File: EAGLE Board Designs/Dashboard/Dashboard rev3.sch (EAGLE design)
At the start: 61 parts, among them J1 AVR-ISP-HEADER, J2 JUMPER0603, X1 CONNECTOR-8NANO, X3 CONNECTOR-4NANO, X4 CONNECTOR-6NANO

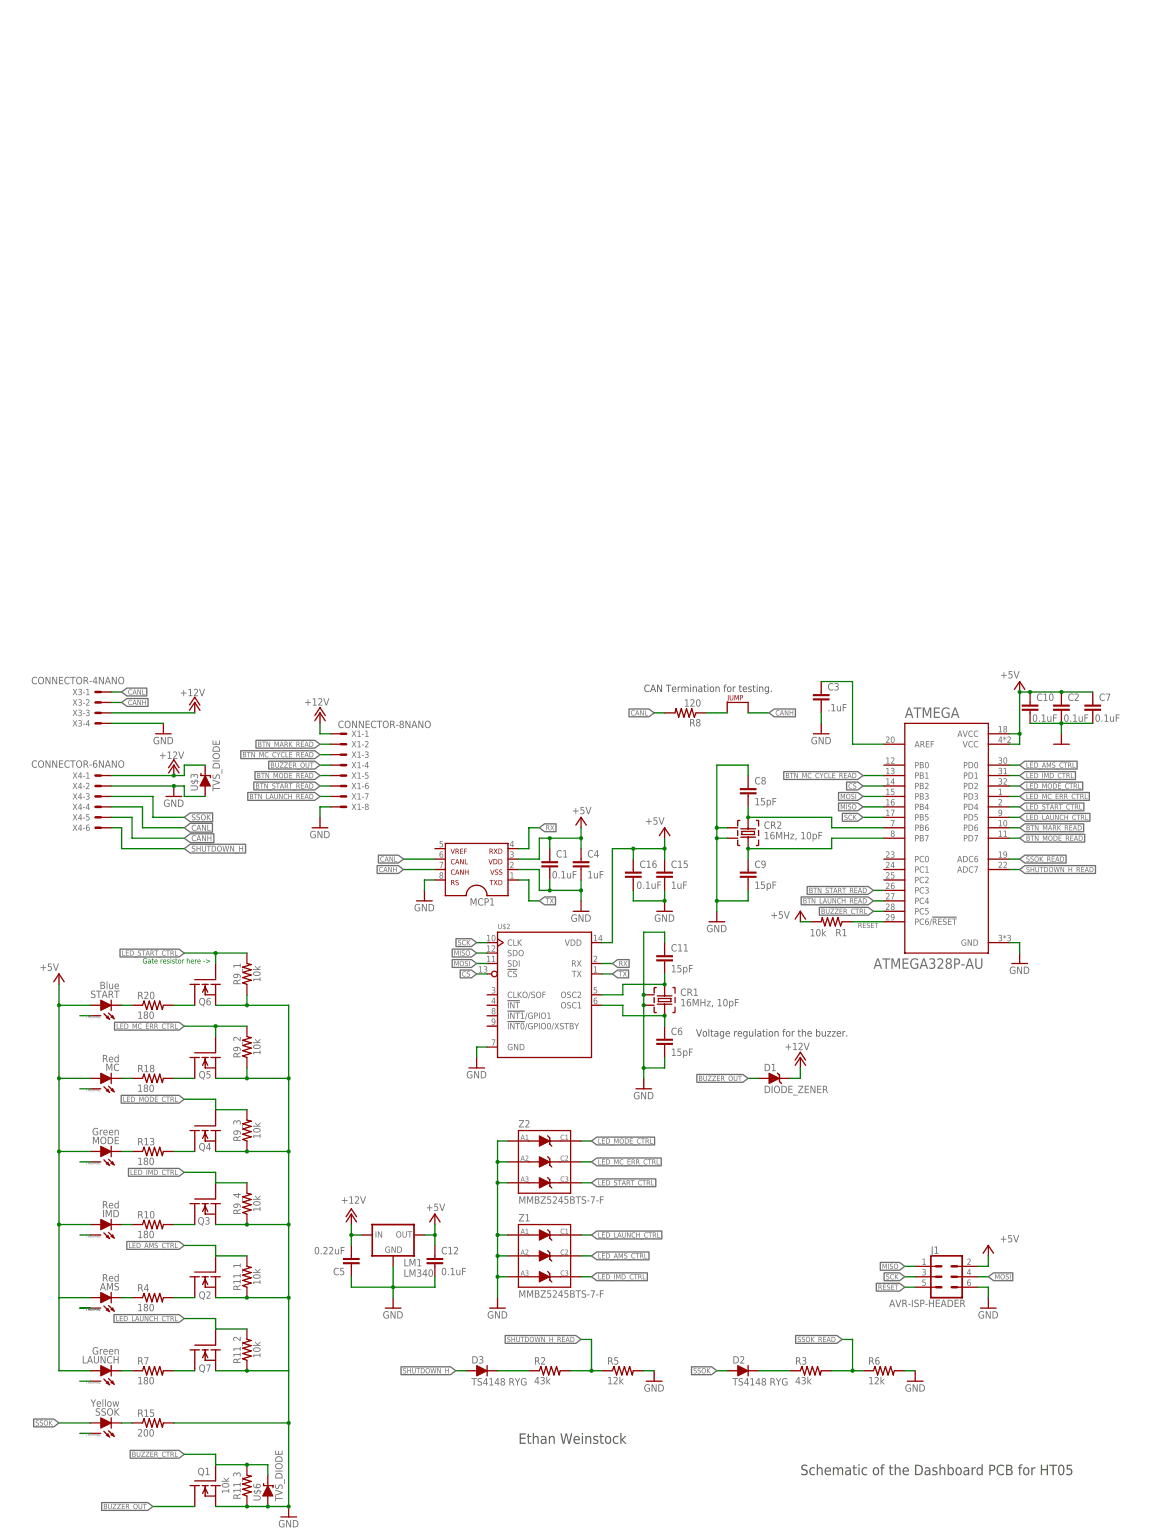
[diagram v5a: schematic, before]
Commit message: MCP 2551 -> MCP2562FD in Rev3 File
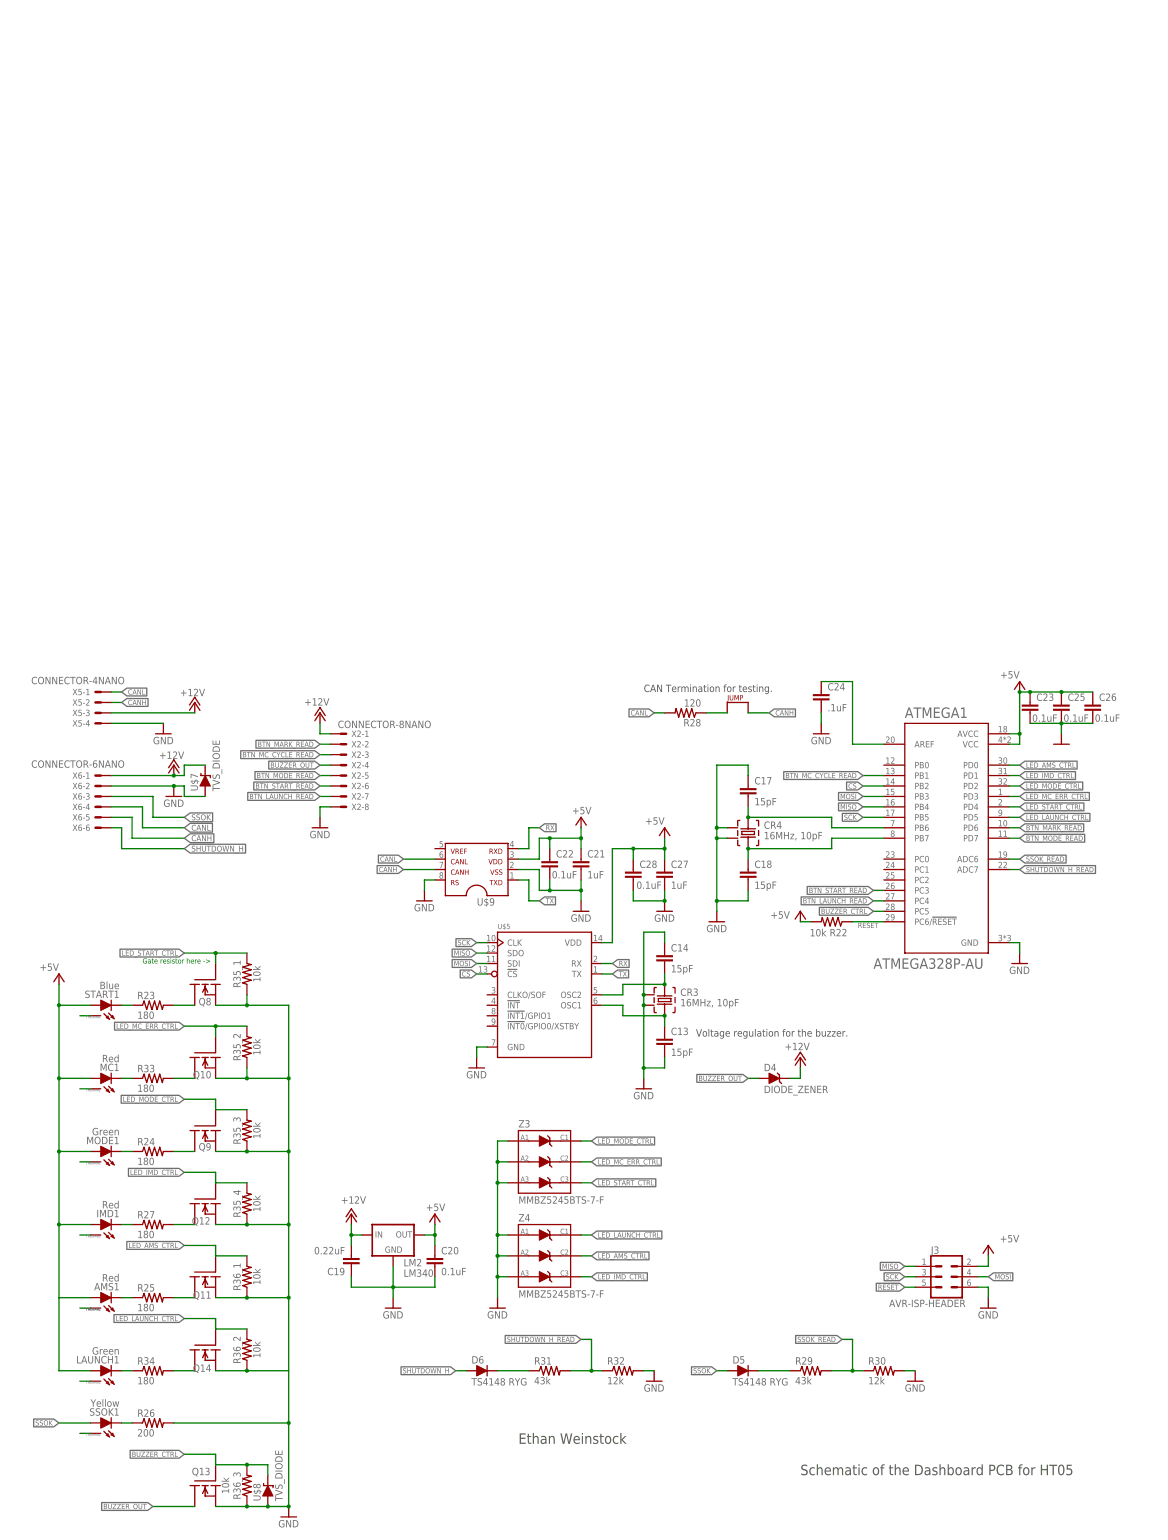
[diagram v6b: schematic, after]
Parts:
- removed MCP1: MCP2551, HyTechDevices:MCP2551
- added U$9: MCP2562FD, HyTechDevices:MCP2562FD
- renumbered AMS to AMS1, ATMEGA to ATMEGA1, C1 to C22, C10 to C23, C11 to C14, C12 to C20, C15 to C27, C16 to C28, C2 to C25, C3 to C24, C4 to C21, C5 to C19, C6 to C13, C7 to C26, C8 to C17, C9 to C18, CR1 to CR3, CR2 to CR4, D1 to D4, D2 to D5, D3 to D6, IMD to IMD1, J1 to J3, J2 to J4, LAUNCH to LAUNCH1, LM1 to LM2, MC to MC1, MODE to MODE1, Q1 to Q13, Q2 to Q11, Q3 to Q12, Q4 to Q9, Q5 to Q10, Q6 to Q8, Q7 to Q14, R1 to R22, R10 to R27, R11 to R36, R13 to R24, R15 to R26, R18 to R33, R2 to R31, R20 to R23, R3 to R29, R4 to R25, R5 to R32, R6 to R30, R7 to R34, R8 to R28, R9 to R35, SSOK to SSOK1, START to START1, U$2 to U$5, U$3 to U$7, U$6 to U$8, X1 to X2, X3 to X5, X4 to X6, Z1 to Z4, Z2 to Z3
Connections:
- net GND1 renamed GND2
- removed net N$30: C14.2, CR3.1, U$5.OSC2
- new net N$42: C14.2, C21.2, C22.2, CR3.1, U$5.OSC2, U$9.2
- net +5V: now also U$9.3; no longer MCP1.3
- net CANH: now also U$9.7; no longer MCP1.7
- net CANL: now also U$9.6; no longer MCP1.6
- net GND: now also U$9.8; no longer C21.2, C22.2, MCP1.2, MCP1.8
- net RX: now also U$9.4; no longer MCP1.4
- net TX: now also U$9.1; no longer MCP1.1

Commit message: Finished changes
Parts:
- removed J3: AVR-ISP-HEADER, HyTechDevices:AVR-ISP-HEADER
- added X1: CONNECTOR-6NANO, HyTechDevices:CONNECTOR-6NANO
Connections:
- net +5V: now also X1-2.S; no longer J3.2
- net GND: now also X1-6.S; no longer J3.6
- net MISO: now also X1-1.S; no longer J3.1
- net MOSI: now also X1-4.S; no longer J3.4
- net RESET: now also X1-5.S; no longer J3.5
- net SCK: now also X1-3.S; no longer J3.3
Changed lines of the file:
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@@
 <part name="C26" library="HyTechDevices" deviceset="CAP" device="0603-CAP" value="0.1uF"/>
 <part name="GND29" library="HyTechSymbols" deviceset="GND" device=""/>
-<part name="J3" library="HyTechDevices" deviceset="AVR-ISP-HEADER" device="" package3d_urn="urn:adsk.eagle:package:22462/2"/>
 <part name="GND30" library="HyTechSymbols" deviceset="GND" device=""/>
 <part name="P+21" library="supply1" library_urn="urn:adsk.eagle:library:371" deviceset="+5V" device=""/>
@@
 <part name="R36" library="HyTechDevices" deviceset="CAT16-*4" device="_1%" technology="F" value="10k"/>
 <part name="U$9" library="HyTechDevices" deviceset="MCP2562FD" device=""/>
+<part name="X1" library="HyTechDevices" deviceset="CONNECTOR-6" device="NANO"/>
 </parts>
 <sheets>
@@
 </instance>
 <instance part="GND29" gate="1" x="259.08" y="193.04" smashed="yes"/>
-<instance part="J3" gate="G$1" x="231.14" y="63.5" smashed="yes">
-<attribute name="VALUE" x="217.17" y="56.134" size="1.778" layer="96"/>
-<attribute name="NAME" x="227.33" y="69.088" size="1.778" layer="95"/>
-</instance>
-<instance part="GND30" gate="1" x="241.3" y="55.88" smashed="yes">
-<attribute name="VALUE" x="238.76" y="53.34" size="1.778" layer="96"/>
-</instance>
-<instance part="P+21" gate="1" x="241.3" y="71.12" smashed="yes">
-<attribute name="VALUE" x="244.094" y="71.882" size="1.778" layer="96"/>
+<instance part="GND30" gate="1" x="236.22" y="86.36" smashed="yes">
+<attribute name="VALUE" x="233.68" y="83.82" size="1.778" layer="96"/>
+</instance>
+<instance part="P+21" gate="1" x="231.14" y="81.28" smashed="yes">
+<attribute name="VALUE" x="228.854" y="82.042" size="1.778" layer="96"/>
 </instance>
 <instance part="D4" gate="G$1" x="190.5" y="111.76" smashed="yes">
@@
 <instance part="U$9" gate="G$1" x="124.46" y="167.64" smashed="yes" rot="R180">
 <attribute name="NAME" x="121.285" y="155.575" size="1.778" layer="95" rot="R180"/>
+</instance>
+<instance part="X1" gate="-1" x="259.08" y="76.2" smashed="yes">
+<attribute name="NAME" x="261.62" y="75.438" size="1.524" layer="95"/>
+<attribute name="VALUE" x="253.238" y="72.517" size="1.778" layer="96"/>
+</instance>
+<instance part="X1" gate="-2" x="259.08" y="78.74" smashed="yes">
+<attribute name="NAME" x="261.62" y="77.978" size="1.524" layer="95"/>
+</instance>
+<instance part="X1" gate="-3" x="259.08" y="81.28" smashed="yes">
+<attribute name="NAME" x="261.62" y="80.518" size="1.524" layer="95"/>
+</instance>
+<instance part="X1" gate="-4" x="259.08" y="83.82" smashed="yes">
+<attribute name="NAME" x="261.62" y="83.058" size="1.524" layer="95"/>
+</instance>
+<instance part="X1" gate="-5" x="259.08" y="86.36" smashed="yes">
+<attribute name="NAME" x="261.62" y="85.598" size="1.524" layer="95"/>
+</instance>
+<instance part="X1" gate="-6" x="259.08" y="88.9" smashed="yes">
+<attribute name="NAME" x="261.62" y="88.138" size="1.524" layer="95"/>
 </instance>
 </instances>
@@
 <pinref part="GND29" gate="1" pin="GND"/>
 <wire x1="259.08" y1="198.12" x2="259.08" y2="195.58" width="0.1524" layer="91"/>
-</segment>
-<segment>
-<pinref part="GND30" gate="1" pin="GND"/>
-<wire x1="241.3" y1="58.42" x2="241.3" y2="60.96" width="0.1524" layer="91"/>
-<pinref part="J3" gate="G$1" pin="6"/>
-<wire x1="241.3" y1="60.96" x2="238.76" y2="60.96" width="0.1524" layer="91"/>
 </segment>
 <segment>
@@
 <pinref part="GND36" gate="1" pin="GND"/>
 </segment>
+<segment>
+<pinref part="X1" gate="-6" pin="S"/>
+<pinref part="GND30" gate="1" pin="GND"/>
+<wire x1="256.54" y1="88.9" x2="236.22" y2="88.9" width="0.1524" layer="91"/>
+</segment>
 </net>
 <net name="+5V" class="0">
@@
 <segment>
 <pinref part="P+21" gate="1" pin="+5V"/>
-<wire x1="241.3" y1="68.58" x2="241.3" y2="66.04" width="0.1524" layer="91"/>
-<pinref part="J3" gate="G$1" pin="2"/>
-<wire x1="241.3" y1="66.04" x2="238.76" y2="66.04" width="0.1524" layer="91"/>
+<pinref part="X1" gate="-2" pin="S"/>
+<wire x1="256.54" y1="78.74" x2="231.14" y2="78.74" width="0.1524" layer="91"/>
 </segment>
 <segment>
@@
 </segment>
 <segment>
-<pinref part="J3" gate="G$1" pin="3"/>
-<wire x1="223.52" y1="63.5" x2="220.98" y2="63.5" width="0.1524" layer="91"/>
-<label x="220.98" y="63.5" size="1.27" layer="95" rot="R180" xref="yes"/>
+<wire x1="256.54" y1="81.28" x2="248.92" y2="81.28" width="0.1524" layer="91"/>
+<label x="248.92" y="81.28" size="1.27" layer="95" rot="R180" xref="yes"/>
+<pinref part="X1" gate="-3" pin="S"/>
 </segment>
 <segment>
@@
 </segment>
 <segment>
-<pinref part="J3" gate="G$1" pin="1"/>
-<wire x1="223.52" y1="66.04" x2="220.98" y2="66.04" width="0.1524" layer="91"/>
-<label x="220.98" y="66.04" size="1.27" layer="95" rot="R180" xref="yes"/>
+<wire x1="256.54" y1="76.2" x2="248.92" y2="76.2" width="0.1524" layer="91"/>
+<label x="248.92" y="76.2" size="1.27" layer="95" rot="R180" xref="yes"/>
+<pinref part="X1" gate="-1" pin="S"/>
 </segment>
 <segment>
@@
 </segment>
 <segment>
-<pinref part="J3" gate="G$1" pin="4"/>
-<wire x1="238.76" y1="63.5" x2="241.3" y2="63.5" width="0.1524" layer="91"/>
-<label x="241.3" y="63.5" size="1.27" layer="95" xref="yes"/>
+<wire x1="256.54" y1="83.82" x2="248.92" y2="83.82" width="0.1524" layer="91"/>
+<label x="248.92" y="83.82" size="1.27" layer="95" rot="R180" xref="yes"/>
+<pinref part="X1" gate="-4" pin="S"/>
 </segment>
 <segment>
@@
 </segment>
 <segment>
-<pinref part="J3" gate="G$1" pin="5"/>
-<wire x1="223.52" y1="60.96" x2="220.98" y2="60.96" width="0.1524" layer="91"/>
-<label x="220.98" y="60.96" size="1.27" layer="95" rot="R180" xref="yes"/>
+<wire x1="256.54" y1="86.36" x2="248.92" y2="86.36" width="0.1524" layer="91"/>
+<label x="248.92" y="86.36" size="1.27" layer="95" rot="R180" xref="yes"/>
+<pinref part="X1" gate="-5" pin="S"/>
 </segment>
 </net>
@@
 will not be understood (or retained) with this version.
 </note>
-<note version="8.3" severity="warning">
-Since Version 8.3, EAGLE supports the association of 3D packages
-with devices in libraries, schematics, and board files. Those 3D
-packages will not be understood (or retained) with this version.
-</note>
 </compatibility>

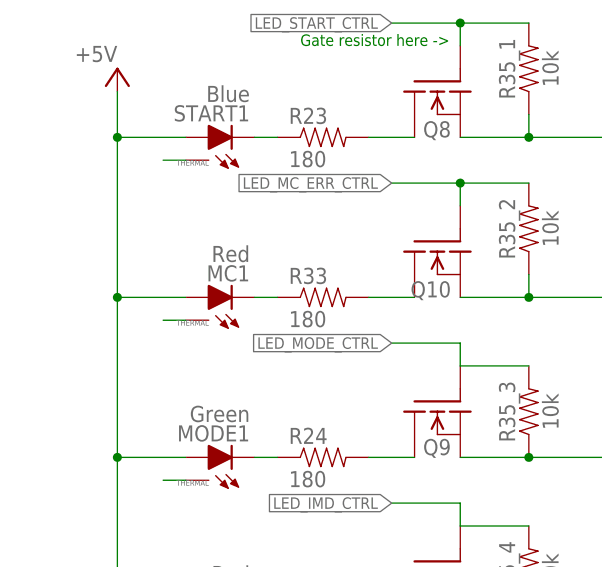
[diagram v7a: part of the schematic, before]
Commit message: Changed MCerror to green
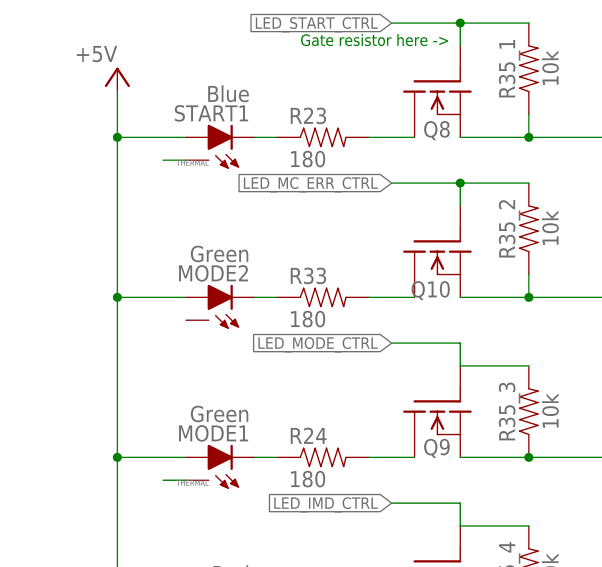
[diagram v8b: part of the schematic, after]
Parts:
- MODE2: value Red -> Green
- renumbered MC1 to MODE2
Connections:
- net THERMAL: no longer MODE2.X
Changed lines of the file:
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@@
 <part name="R28" library="HyTechDevices" deviceset="RESISTOR" device="0603-RES" value="120"/>
 <part name="GND31" library="HyTechSymbols" deviceset="GND" device=""/>
-<part name="MC1" library="HyTechDevices" deviceset="XP-E2" device="XP-E2" value="Red"/>
 <part name="START1" library="HyTechDevices" deviceset="XP-E2" device="XP-E2" value="Blue"/>
 <part name="MODE1" library="HyTechDevices" deviceset="XP-E2" device="XP-E2" value="Green"/>
@@
 <part name="U$9" library="HyTechDevices" deviceset="MCP2562FD" device=""/>
 <part name="X1" library="HyTechDevices" deviceset="CONNECTOR-6" device="NANO"/>
+<part name="MODE2" library="HyTechDevices" deviceset="XP-E2" device="XP-E2" value="Green"/>
 </parts>
 <sheets>
@@
 <attribute name="VALUE" x="68.58" y="2.54" size="1.778" layer="96"/>
 </instance>
-<instance part="MC1" gate="G$1" x="25.4" y="111.76" smashed="yes" rot="R90">
-<attribute name="NAME" x="29.972" y="115.316" size="1.778" layer="95" rot="R180"/>
-<attribute name="VALUE" x="29.972" y="117.475" size="1.778" layer="96" rot="R180"/>
-</instance>
 <instance part="START1" gate="G$1" x="25.4" y="129.54" smashed="yes" rot="R90">
 <attribute name="NAME" x="29.972" y="133.096" size="1.778" layer="95" rot="R180"/>
@@
 <instance part="X1" gate="-6" x="259.08" y="88.9" smashed="yes">
 <attribute name="NAME" x="261.62" y="88.138" size="1.524" layer="95"/>
+</instance>
+<instance part="MODE2" gate="G$1" x="25.4" y="111.76" smashed="yes" rot="R90">
+<attribute name="NAME" x="29.972" y="115.316" size="1.778" layer="95" rot="R180"/>
+<attribute name="VALUE" x="29.972" y="117.475" size="1.778" layer="96" rot="R180"/>
 </instance>
 </instances>
@@
 </segment>
 <segment>
-<pinref part="MC1" gate="G$1" pin="X"/>
-<wire x1="22.86" y1="109.22" x2="20.32" y2="109.22" width="0.1524" layer="91"/>
-<label x="25.4" y="109.22" size="0.6096" layer="95" rot="R180"/>
-</segment>
-<segment>
 <pinref part="MODE1" gate="G$1" pin="X"/>
 <wire x1="22.86" y1="91.44" x2="20.32" y2="91.44" width="0.1524" layer="91"/>
@@
 <wire x1="15.24" y1="76.2" x2="15.24" y2="93.98" width="0.1524" layer="91"/>
 <wire x1="15.24" y1="93.98" x2="15.24" y2="111.76" width="0.1524" layer="91"/>
+<pinref part="P+19" gate="1" pin="+5V"/>
 <wire x1="15.24" y1="111.76" x2="15.24" y2="129.54" width="0.1524" layer="91"/>
-<pinref part="P+19" gate="1" pin="+5V"/>
 <wire x1="15.24" y1="129.54" x2="15.24" y2="134.62" width="0.1524" layer="91"/>
-<wire x1="15.24" y1="111.76" x2="22.86" y2="111.76" width="0.1524" layer="91"/>
-<junction x="15.24" y="111.76"/>
 <wire x1="22.86" y1="93.98" x2="15.24" y2="93.98" width="0.1524" layer="91"/>
 <junction x="15.24" y="93.98"/>
@@
 <junction x="15.24" y="129.54"/>
 <pinref part="START1" gate="G$1" pin="A"/>
-<pinref part="MC1" gate="G$1" pin="A"/>
 <pinref part="MODE1" gate="G$1" pin="A"/>
 <pinref part="IMD1" gate="G$1" pin="A"/>
 <pinref part="AMS1" gate="G$1" pin="A"/>
+<pinref part="MODE2" gate="G$1" pin="A"/>
+<wire x1="22.86" y1="111.76" x2="15.24" y2="111.76" width="0.1524" layer="91"/>
+<junction x="15.24" y="111.76"/>
 </segment>
 </net>
@@
 <wire x1="33.02" y1="58.42" x2="30.48" y2="58.42" width="0.1524" layer="91"/>
 <pinref part="AMS1" gate="G$1" pin="C"/>
-</segment>
-</net>
-<net name="N$28" class="0">
-<segment>
-<pinref part="MC1" gate="G$1" pin="C"/>
-<pinref part="R33" gate="G$1" pin="1"/>
-<wire x1="30.48" y1="111.76" x2="33.02" y2="111.76" width="0.1524" layer="91"/>
 </segment>
 </net>
@@
 </segment>
 </net>
+<net name="N$2" class="0">
+<segment>
+<pinref part="R33" gate="G$1" pin="1"/>
+<pinref part="MODE2" gate="G$1" pin="C"/>
+<wire x1="33.02" y1="111.76" x2="30.48" y2="111.76" width="0.1524" layer="91"/>
+</segment>
+</net>
